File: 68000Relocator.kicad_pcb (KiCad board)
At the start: 2 copper layers, 97.8 x 97.4 mm, 2 parts, among them U1 68000D, U2 68000D

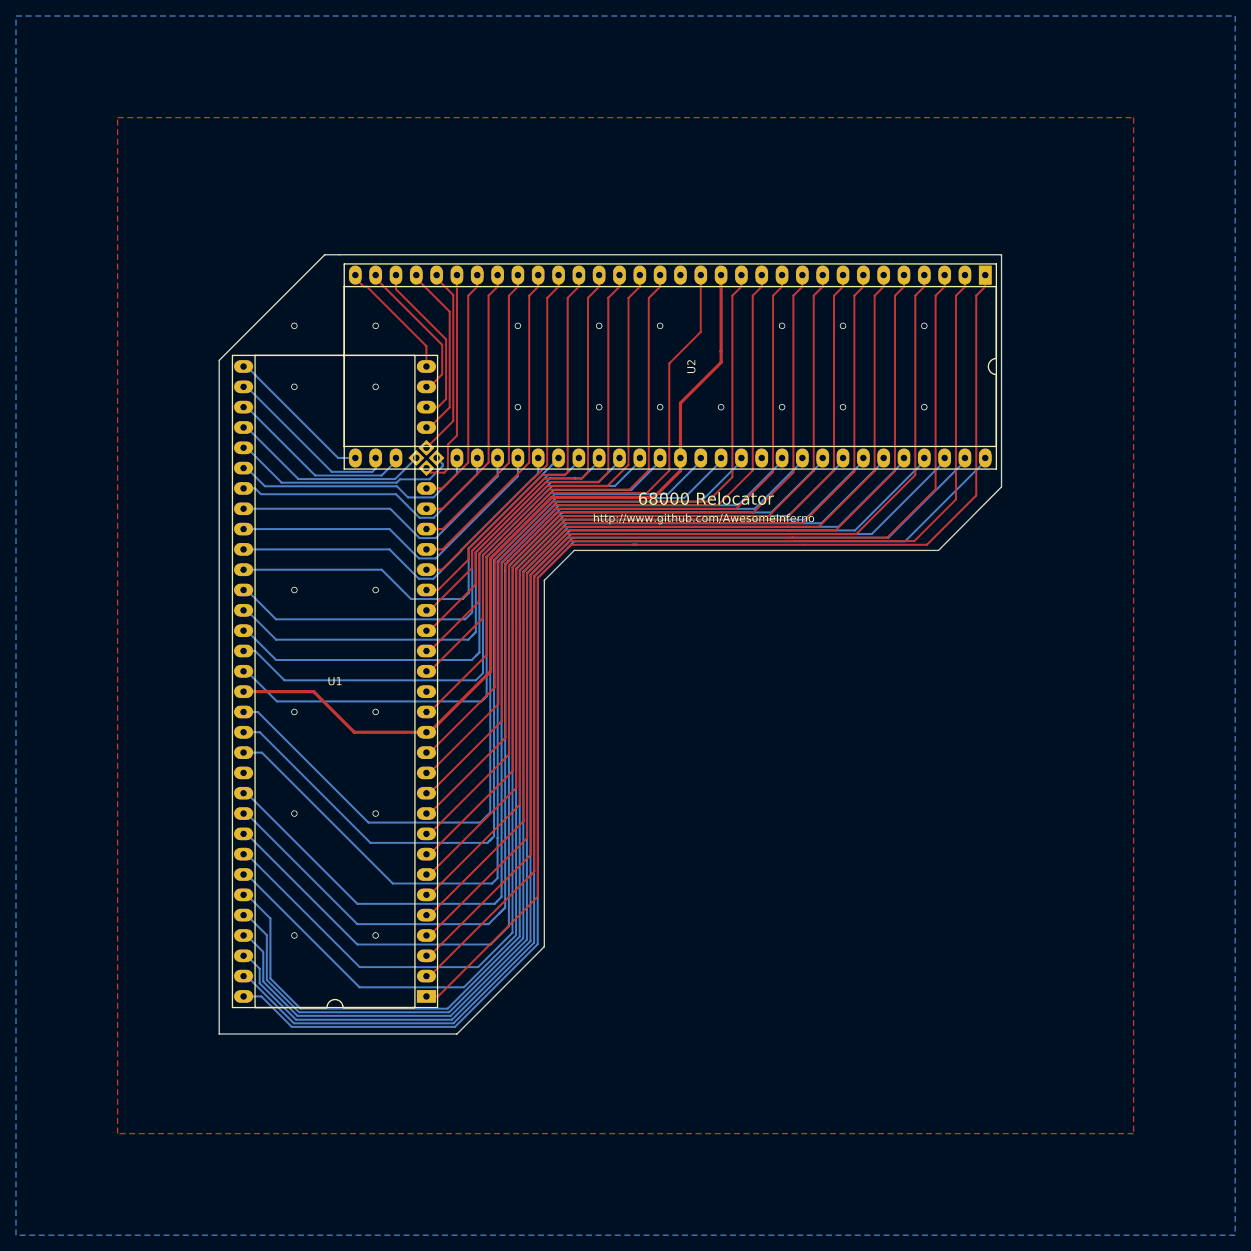
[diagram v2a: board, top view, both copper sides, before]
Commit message: Make both slopes equal in length
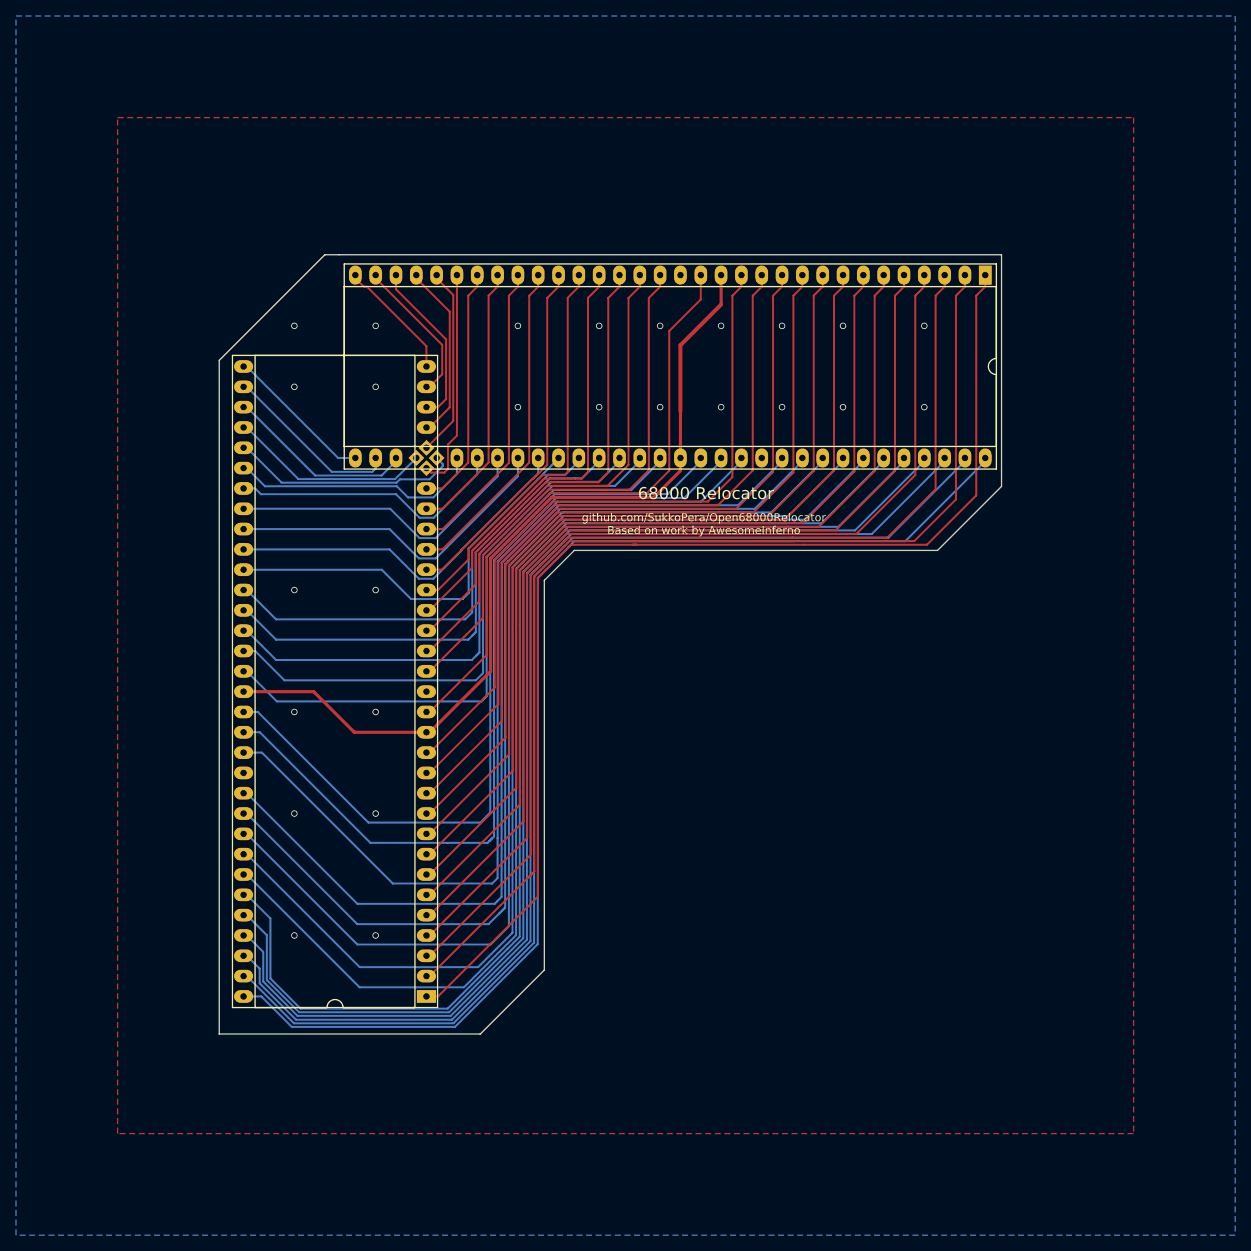
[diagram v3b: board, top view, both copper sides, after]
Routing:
- net GND: vias 25 -> 26
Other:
- outline, holes or cut-outs redrawn
- board text added: "github.com/SukkoPera/Open68000Relocator Based on work by AwesomeInferno"
- board text removed: "http://www.github.com/AwesomeInferno"
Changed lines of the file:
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@@
     (thickness 1.6)
     (drawings 18)
-    (tracks 586)
+    (tracks 587)
     (zones 0)
     (modules 2)
@@
     (descr "64-lead dip package, row spacing 22.86 mm (900 mils), Socket, LongPads")
     (tags "DIL DIP PDIP 2.54mm 22.86mm 900mil Socket LongPads")
-    (fp_text reference U2 (at 11.43 36.703 270) (layer F.SilkS)
+    (fp_text reference U2 (at 11.43 36.703 270) (layer F.Fab)
       (effects (font (size 1 1) (thickness 0.15)))
     )
@@
       (rotate (xyz 0 0 0))
     )
+    (model ${KISYS3DMOD}/Package_DIP.3dshapes/DIP-64_W15.24mm.step
+      (at (xyz 0 0 0))
+      (scale (xyz 1.5 1 1))
+      (rotate (xyz 0 0 0))
+    )
   )
   (module Housings_DIP:DIP-64_W22.86mm_Socket_LongPads (layer F.Cu)
@@
     (descr "64-lead dip package, row spacing 22.86 mm (900 mils), Socket, LongPads")
     (tags "DIL DIP PDIP 2.54mm 22.86mm 900mil Socket LongPads")
-    (fp_text reference U1 (at 11.43 39.37 180) (layer F.SilkS)
+    (fp_text reference U1 (at 11.43 39.37 180) (layer F.Fab)
       (effects (font (size 1 1) (thickness 0.15)))
     )
@@
     (pad 64 thru_hole oval (at 22.86 0 180) (size 2.4 1.6) (drill 0.8) (layers *.Cu *.Mask)
       (net 62 /D5))
-    (model Housings_DIP.3dshapes/DIP-64_W22.86mm_Socket_LongPads.wrl
-      (at (xyz 0 0 0))
+    (model ${KISYS3DMOD}/Connector_PinHeader_2.54mm.3dshapes/PinHeader_1x32_P2.54mm_Vertical.wrl
+      (offset (xyz 0 0 -2))
       (scale (xyz 1 1 1))
-      (rotate (xyz 0 0 0))
+      (rotate (xyz 0 180 0))
     )
-  )
+    (model ${KISYS3DMOD}/Connector_PinHeader_2.54mm.3dshapes/PinHeader_1x32_P2.54mm_Vertical.wrl
+      (offset (xyz 22.9 0 -2))
+      (scale (xyz 1 1 1))
+      (rotate (xyz 0 180 0))
+    )
+  )
+  (gr_line (start 121.793 144.653) (end 129.794 136.652) (layer Edge.Cuts) (width 0.15))
   (dimension 97.79 (width 0.3) (layer F.Fab)
     (gr_text "97,790 mm" (at 138.049 39.429) (layer F.Fab)
@@
   )
   (gr_line (start 129.794 87.9475) (end 133.5405 84.201) (layer Edge.Cuts) (width 0.15))
-  (gr_line (start 186.944 76.2635) (end 186.944 74.168) (layer Edge.Cuts) (width 0.15))
-  (gr_line (start 179.07 84.201) (end 186.944 76.2635) (layer Edge.Cuts) (width 0.15))
-  (gr_line (start 133.5405 84.201) (end 179.07 84.201) (layer Edge.Cuts) (width 0.15))
-  (gr_line (start 129.794 133.731) (end 129.794 87.9475) (layer Edge.Cuts) (width 0.15))
-  (gr_line (start 118.872 144.653) (end 129.794 133.731) (layer Edge.Cuts) (width 0.15))
+  (gr_line (start 186.944 76.2) (end 186.944 74.168) (layer Edge.Cuts) (width 0.15))
+  (gr_line (start 178.943 84.201) (end 186.944 76.2) (layer Edge.Cuts) (width 0.15))
+  (gr_line (start 133.5405 84.201) (end 178.943 84.201) (layer Edge.Cuts) (width 0.15))
+  (gr_line (start 129.794 136.652) (end 129.794 87.9475) (layer Edge.Cuts) (width 0.15))
   (gr_line (start 102.362 47.244) (end 104.14 47.244) (layer Edge.Cuts) (width 0.15))
   (gr_line (start 89.154 60.452) (end 102.362 47.244) (layer Edge.Cuts) (width 0.15))
-  (gr_line (start 118.872 144.653) (end 89.154 144.653) (layer Edge.Cuts) (width 0.15))
+  (gr_line (start 121.793 144.653) (end 89.154 144.653) (layer Edge.Cuts) (width 0.15))
   (gr_line (start 186.944 47.244) (end 186.944 74.168) (layer Edge.Cuts) (width 0.15))
   (gr_line (start 104.14 47.244) (end 186.944 47.244) (layer Edge.Cuts) (width 0.15))
   (gr_line (start 89.154 144.653) (end 89.154 60.452) (layer Edge.Cuts) (width 0.15))
-  (gr_text http://www.github.com/AwesomeInferno (at 149.733 80.2005) (layer F.SilkS)
+  (gr_text "github.com/SukkoPera/Open68000Relocator\nBased on work by AwesomeInferno" (at 149.733 80.899) (layer F.SilkS)
     (effects (font (size 1 1) (thickness 0.2)))
   )
-  (gr_text "68000 Relocator" (at 149.987 77.7875) (layer F.SilkS)
+  (gr_text "68000 Relocator" (at 149.987 77.089) (layer F.SilkS)
     (effects (font (size 1.5 1.5) (thickness 0.3)))
   )
@@
   (segment (start 130.716557 77.566034) (end 123.076797 85.205794) (width 0.4) (layer F.Cu) (net 27))
   (segment (start 123.076797 85.205794) (end 123.076797 99.319203) (width 0.4) (layer F.Cu) (net 27))
-  (segment (start 151.892 60.706) (end 151.892 59.309) (width 0.4) (layer F.Cu) (net 27) (status 40000))
-  (segment (start 151.892 59.309) (end 151.892 49.784) (width 0.4) (layer F.Cu) (net 27) (status 40000))
-  (segment (start 146.812 65.786) (end 151.892 60.706) (width 0.4) (layer F.Cu) (net 27) (status 40000))
-  (segment (start 146.812 72.644) (end 146.812 65.786) (width 0.4) (layer F.Cu) (net 27) (status 40000))
+  (segment (start 146.812 58.547) (end 151.892 53.467) (width 0.5) (layer F.Cu) (net 27))
+  (segment (start 151.892 53.467) (end 151.892 49.784) (width 0.4) (layer F.Cu) (net 27))
+  (segment (start 146.812 66.802) (end 146.812 58.547) (width 0.5) (layer F.Cu) (net 27))
+  (segment (start 146.812 72.644) (end 146.812 66.802) (width 0.4) (layer F.Cu) (net 27))
   (segment (start 96.26701 97.89901) (end 92.602 94.234) (width 0.25) (layer B.Cu) (net 28))
   (segment (start 92.602 94.234) (end 92.202 94.234) (width 0.25) (layer B.Cu) (net 28))
@@
   (segment (start 139.192 73.044) (end 136.601989 75.634011) (width 0.25) (layer B.Cu) (net 28))
   (segment (start 121.682533 96.947967) (end 121.285 97.3455) (width 0.25) (layer B.Cu) (net 28))
-  (segment (start 149.352 56.896) (end 149.352 49.784) (width 0.25) (layer F.Cu) (net 29) (status 40000))
-  (segment (start 145.415 60.833) (end 149.352 56.896) (width 0.25) (layer F.Cu) (net 29) (status 40000))
-  (segment (start 145.415 74.2315) (end 145.415 60.833) (width 0.25) (layer F.Cu) (net 29) (status 40000))
-  (segment (start 115.062 104.394) (end 115.462 104.394) (width 0.25) (layer F.Cu) (net 29))
-  (segment (start 115.462 104.394) (end 122.551786 97.304214) (width 0.25) (layer F.Cu) (net 29))
-  (segment (start 122.551786 97.304214) (end 122.551786 84.988328) (width 0.25) (layer F.Cu) (net 29))
-  (segment (start 122.551786 84.988328) (end 130.499091 77.041023) (width 0.25) (layer F.Cu) (net 29))
-  (segment (start 130.499091 77.041023) (end 142.605477 77.041023) (width 0.25) (layer F.Cu) (net 29))
-  (segment (start 142.605477 77.041023) (end 145.415 74.2315) (width 0.25) (layer F.Cu) (net 29))
+  (segment (start 122.551786 97.304214) (end 115.462 104.394) (width 0.25) (layer F.Cu) (net 29))
+  (segment (start 122.551786 84.988328) (end 122.551786 97.304214) (width 0.25) (layer F.Cu) (net 29))
+  (segment (start 130.499091 77.041023) (end 122.551786 84.988328) (width 0.25) (layer F.Cu) (net 29))
+  (segment (start 145.415 74.2315) (end 142.605477 77.041023) (width 0.25) (layer F.Cu) (net 29))
+  (segment (start 115.462 104.394) (end 115.062 104.394) (width 0.25) (layer F.Cu) (net 29))
+  (segment (start 142.605477 77.041023) (end 130.499091 77.041023) (width 0.25) (layer F.Cu) (net 29))
+  (segment (start 149.352 52.832) (end 149.352 49.784) (width 0.25) (layer F.Cu) (net 29))
+  (segment (start 145.415 56.769) (end 149.352 52.832) (width 0.25) (layer F.Cu) (net 29))
+  (segment (start 145.415 56.769) (end 145.415 74.2315) (width 0.25) (layer F.Cu) (net 29))
   (segment (start 93.652 96.774) (end 92.202 96.774) (width 0.25) (layer B.Cu) (net 30))
   (segment (start 97.31701 100.43901) (end 93.652 96.774) (width 0.25) (layer B.Cu) (net 30))
@@
   (via (at 98.552 56.134) (size 0.8) (drill 0.6) (layers F.Cu B.Cu) (net 31))
   (via (at 108.712 56.134) (size 0.8) (drill 0.6) (layers F.Cu B.Cu) (net 31))
+  (via (at 151.892 56.134) (size 0.8) (drill 0.6) (layers F.Cu B.Cu) (net 31))
   (segment (start 96.36701 103.07901) (end 92.602 99.314) (width 0.25) (layer B.Cu) (net 32))
   (segment (start 92.602 99.314) (end 92.202 99.314) (width 0.25) (layer B.Cu) (net 32))

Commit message: Get rid of ground loop
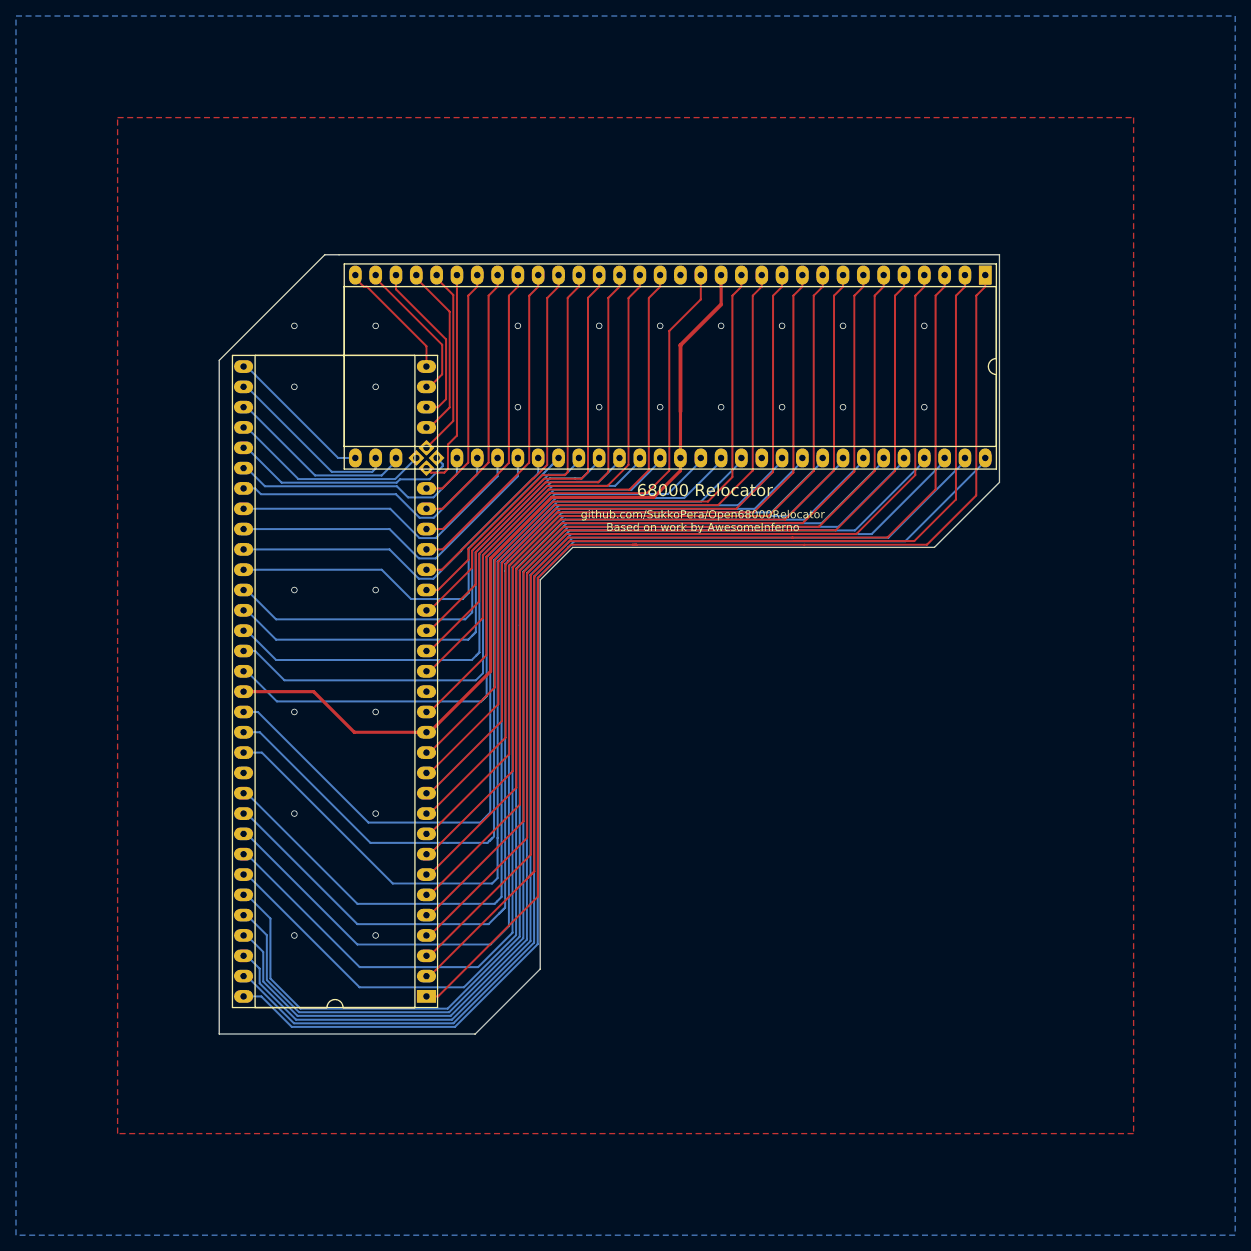
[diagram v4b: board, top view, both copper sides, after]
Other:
- board size 97.8 x 97.4 mm -> 97.5 x 97.4 mm
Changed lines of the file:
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@@
   (general
     (thickness 1.6)
-    (drawings 18)
+    (drawings 17)
     (tracks 587)
     (zones 0)
@@
     (pad 64 thru_hole oval (at 22.86 0 270) (size 2.4 1.6) (drill 0.8) (layers *.Cu *.Mask)
       (net 62 /D5))
-    (model Housings_DIP.3dshapes/DIP-64_W22.86mm_Socket_LongPads.wrl
+    (model ${KISYS3DMOD}/Package_DIP.3dshapes/DIP-64_W15.24mm.step
+      (offset (xyz 0 0 5.5))
+      (scale (xyz 1.5 1 1.3))
+      (rotate (xyz 0 0 0))
+    )
+    (model ${KISYS3DMOD}/Package_DIP.3dshapes/DIP-64_W15.24mm_Socket.step
       (at (xyz 0 0 0))
-      (scale (xyz 1 1 1))
-      (rotate (xyz 0 0 0))
-    )
-    (model ${KISYS3DMOD}/Package_DIP.3dshapes/DIP-64_W15.24mm.step
-      (at (xyz 0 0 0))
-      (scale (xyz 1.5 1 1))
+      (scale (xyz 1.5 1 1.3))
       (rotate (xyz 0 0 0))
     )
@@
     )
   )
-  (gr_line (start 121.793 144.653) (end 129.794 136.652) (layer Edge.Cuts) (width 0.15))
-  (dimension 97.79 (width 0.3) (layer F.Fab)
-    (gr_text "97,790 mm" (at 138.049 39.429) (layer F.Fab)
+  (gr_line (start 121.158 144.653) (end 129.286 136.525) (layer Edge.Cuts) (width 0.15))
+  (dimension 97.536 (width 0.3) (layer F.Fab)
+    (gr_text "97,536 mm" (at 137.922 39.429) (layer F.Fab)
       (effects (font (size 1.5 1.5) (thickness 0.3)))
     )
-    (feature1 (pts (xy 186.944 47.244) (xy 186.944 40.942579)))
+    (feature1 (pts (xy 186.69 47.244) (xy 186.69 40.942579)))
     (feature2 (pts (xy 89.154 47.244) (xy 89.154 40.942579)))
-    (crossbar (pts (xy 89.154 41.529) (xy 186.944 41.529)))
-    (arrow1a (pts (xy 186.944 41.529) (xy 185.817496 42.115421)))
-    (arrow1b (pts (xy 186.944 41.529) (xy 185.817496 40.942579)))
+    (crossbar (pts (xy 89.154 41.529) (xy 186.69 41.529)))
+    (arrow1a (pts (xy 186.69 41.529) (xy 185.563496 42.115421)))
+    (arrow1b (pts (xy 186.69 41.529) (xy 185.563496 40.942579)))
     (arrow2a (pts (xy 89.154 41.529) (xy 90.280504 42.115421)))
     (arrow2b (pts (xy 89.154 41.529) (xy 90.280504 40.942579)))
@@
     (arrow2b (pts (xy 82.886606 47.172543) (xy 83.473027 48.299047)))
   )
-  (gr_line (start 129.794 87.9475) (end 133.5405 84.201) (layer Edge.Cuts) (width 0.15))
-  (gr_line (start 186.944 76.2) (end 186.944 74.168) (layer Edge.Cuts) (width 0.15))
-  (gr_line (start 178.943 84.201) (end 186.944 76.2) (layer Edge.Cuts) (width 0.15))
-  (gr_line (start 133.5405 84.201) (end 178.943 84.201) (layer Edge.Cuts) (width 0.15))
-  (gr_line (start 129.794 136.652) (end 129.794 87.9475) (layer Edge.Cuts) (width 0.15))
+  (gr_line (start 129.286 87.884) (end 133.35 83.82) (layer Edge.Cuts) (width 0.15))
+  (gr_line (start 178.562 83.82) (end 186.69 75.692) (layer Edge.Cuts) (width 0.15))
+  (gr_line (start 133.35 83.82) (end 178.562 83.82) (layer Edge.Cuts) (width 0.15))
+  (gr_line (start 129.286 136.525) (end 129.286 87.884) (layer Edge.Cuts) (width 0.15))
   (gr_line (start 102.362 47.244) (end 104.14 47.244) (layer Edge.Cuts) (width 0.15))
   (gr_line (start 89.154 60.452) (end 102.362 47.244) (layer Edge.Cuts) (width 0.15))
-  (gr_line (start 121.793 144.653) (end 89.154 144.653) (layer Edge.Cuts) (width 0.15))
-  (gr_line (start 186.944 47.244) (end 186.944 74.168) (layer Edge.Cuts) (width 0.15))
-  (gr_line (start 104.14 47.244) (end 186.944 47.244) (layer Edge.Cuts) (width 0.15))
+  (gr_line (start 121.158 144.653) (end 89.154 144.653) (layer Edge.Cuts) (width 0.15))
+  (gr_line (start 186.69 47.244) (end 186.69 75.692) (layer Edge.Cuts) (width 0.15))
+  (gr_line (start 104.14 47.244) (end 186.69 47.244) (layer Edge.Cuts) (width 0.15))
   (gr_line (start 89.154 144.653) (end 89.154 60.452) (layer Edge.Cuts) (width 0.15))
-  (gr_text "github.com/SukkoPera/Open68000Relocator\nBased on work by AwesomeInferno" (at 149.733 80.899) (layer F.SilkS)
+  (gr_text "github.com/SukkoPera/Open68000Relocator\nBased on work by AwesomeInferno" (at 149.606 80.518) (layer F.SilkS)
     (effects (font (size 1 1) (thickness 0.2)))
   )
-  (gr_text "68000 Relocator" (at 149.987 77.089) (layer F.SilkS)
+  (gr_text "68000 Relocator" (at 149.86 76.708) (layer F.SilkS)
     (effects (font (size 1.5 1.5) (thickness 0.3)))
   )
